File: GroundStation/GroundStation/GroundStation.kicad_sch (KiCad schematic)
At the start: 72 parts, among them J1 SD_Card_Receptacle, J4 Conn_Coaxial, J5 Conn_01x02, P1 USB_C_Plug_USB2.0, Q1 TSM3481CX6 RFG, U1 STM32F103C8Tx, U10 E22-400T30S, U101 LD1117S33TR_SOT223, U11 E80-900M23313S, U4 TPS54538RQFR, U9 NEO-M9N-00B

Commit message: second need freerouting
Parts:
- P1: footprint Connector_USB:USB3_A_Molex_48393-001 -> Connector_USB:USB_C_Receptacle_JAE_DX07S016JA1R1500
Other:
- moved on the sheet: C12, C13, C14, C15, C16, C17, C18, C19, L1, R1, R13, R14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

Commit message: 4/20grounglast
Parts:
- removed C12: 100n, Capacitor_SMD:C_0805_2012Metric_Pad1.18x1.45mm_HandSolder, symbol Device:C
- removed C13, C14, C15: 4.7u, Capacitor_SMD:C_0805_2012Metric_Pad1.18x1.45mm_HandSolder, symbol Device:C
- removed C16: 10p, Capacitor_SMD:C_0805_2012Metric_Pad1.18x1.45mm_HandSolder, symbol Device:C
- removed C17, C18, C19: 47u, Capacitor_SMD:C_0805_2012Metric_Pad1.18x1.45mm_HandSolder, symbol Device:C
- removed C41: NC, Capacitor_SMD:C_0805_2012Metric_Pad1.18x1.45mm_HandSolder, symbol Device:C
- removed C42: 100p, Capacitor_SMD:C_0805_2012Metric_Pad1.18x1.45mm_HandSolder, symbol Device:C
- removed D102, D103: TVS, Diode_SMD:D_SOD-123, symbol Device:D_TVS_Filled
- removed L1: 6.8u, Inductor_SMD:L_0805_2012Metric_Pad1.05x1.20mm_HandSolder, symbol Device:L
- removed L2: short, Inductor_SMD:L_Bourns_SDR0604, symbol Device:L
- removed R1: 390k, Resistor_SMD:R_0805_2012Metric_Pad1.20x1.40mm_HandSolder, symbol Device:R
- removed R13: 18k, Resistor_SMD:R_0805_2012Metric_Pad1.20x1.40mm_HandSolder, symbol Device:R
- removed R14: 220k, Resistor_SMD:R_0805_2012Metric_Pad1.20x1.40mm_HandSolder, symbol Device:R
- removed R15: 30k, Resistor_SMD:R_0805_2012Metric_Pad1.20x1.40mm_HandSolder, symbol Device:R
- removed R16(PG_pull_up)101, R2: 100k, Resistor_SMD:R_0805_2012Metric_Pad1.20x1.40mm_HandSolder, symbol Device:R
- removed R27: NC, Resistor_SMD:R_0805_2012Metric_Pad1.20x1.40mm_HandSolder, symbol Device:R
- removed U4: TPS54538RQFR, RF:TPS54538RQFR, symbol Small_av_tony_lib:TPS54538RQFR
- added BU101: ~, Connector:FanPinHeader_1x03_P2.54mm_Vertical, symbol New_Library_0:BK
- added C101: 330u, Capacitor_SMD:C_0805_2012Metric_Pad1.18x1.45mm_HandSolder, symbol Device:C
- added C102: 22u, Capacitor_SMD:C_0805_2012Metric_Pad1.18x1.45mm_HandSolder, symbol Device:C
- added C103: 2.2u, Capacitor_SMD:C_0805_2012Metric_Pad1.18x1.45mm_HandSolder, symbol Device:C
- added C104: 1u, Capacitor_SMD:C_0805_2012Metric_Pad1.18x1.45mm_HandSolder, symbol Device:C
- added C27, C28: 22pF, Capacitor_SMD:C_0603_1608Metric_Pad1.08x0.95mm_HandSolder, symbol Device:C
- added D102, D104: D_Schottky, Diode_SMD:D_SMA, symbol Device:D_Schottky
- added H101, H102, H103: MountingHole, MountingHole:MountingHole_3.2mm_M3, symbol Mechanical:MountingHole
- added L101, L102: 1mH, Inductor_SMD:L_0805_2012Metric_Pad1.05x1.20mm_HandSolder, symbol Device:L
- added Y1: 8Mhz, Crystal:Crystal_SMD_5032-4Pin_5.0x3.2mm, symbol Device:Crystal_GND24
- J4: footprint Connector_Coaxial:BNC_Amphenol_B6252HB-NPP3G-50_Horizontal -> Connector_Coaxial:U.FL_Hirose_U.FL-R-SMT-1_Vertical
- J5: footprint Connector_PinHeader_2.54mm:PinHeader_1x02_P2.54mm_Horizontal -> Connector_Molex:Molex_Micro-Fit_3.0_43650-0200_1x02_P3.00mm_Horizontal
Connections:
- net +3.3V: now also C10.1, C2.1, C39.1, C40.1, C6.1, C7.1, C8.1, C9.1, J1.4 (VDD), R29.1, R2_up1.1, U1.1 (VBAT), U1.24 (VDD), U1.36 (VDD), U1.48 (VDD), U9.22 (V_BCKP), U9.23 (VCC)
- net BUCK_5V: now also BU101.3 (VOUT), C102.1, D102.2 (A)
- net GND: now also BU101.2 (GND), C102.2, C104.2, C27.2, C28.2, L102.2, Y1.2 (G), Y1.4 (G)
- net USB_5V: now also D104.2 (A)
- net V_BAT+: now also C101.1, C103.1, L101.1
- net HSE_IN: now reaches U1.10 (PA0)
- net HSE_IN: now also C27.1, Y1.1
- net HSE_OUT: now reaches U1.11 (PA1)
- net HSE_OUT: now also C28.1, Y1.3
- net at J4.1 (In): now also U9.11 (RF_IN)
- net at C23.1, U101.3 (VI): now also D102.1 (K), D104.1 (K)
- removed net 3.3V: C10.1, C2.1, C39.1, C40.1, C6.1, C7.1, C8.1, C9.1, FB1.2, J1.4 (VDD), R29.1, R2_up1.1, U1.1 (VBAT), U1.24 (VDD), U1.36 (VDD), U1.48 (VDD), U9.22 (V_BCKP), U9.23 (VCC)
- new net: BU101.1 (VIN), C104.1, L101.2
- new net: C101.2, C103.2, L102.1
- no-connect marks 47 -> 45
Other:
- note added: "HSE crystal"
- moved on the sheet: J4

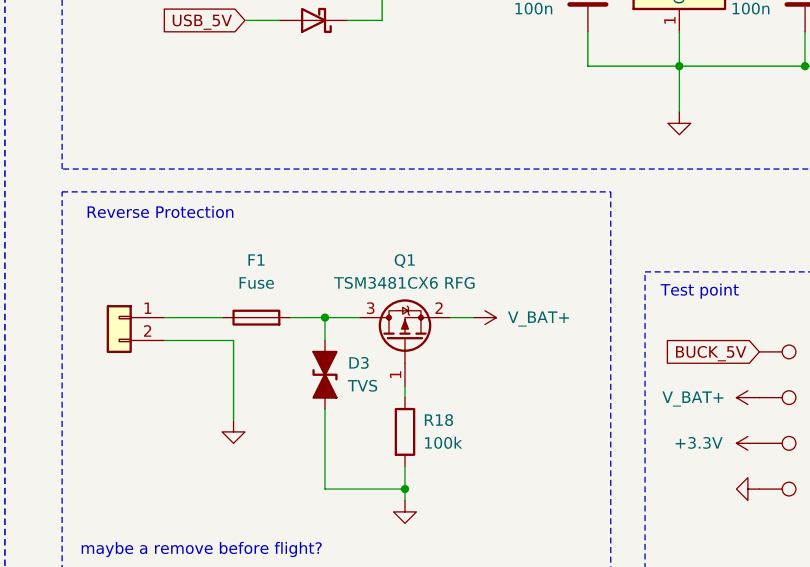
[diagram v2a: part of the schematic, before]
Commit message: change GS MOS
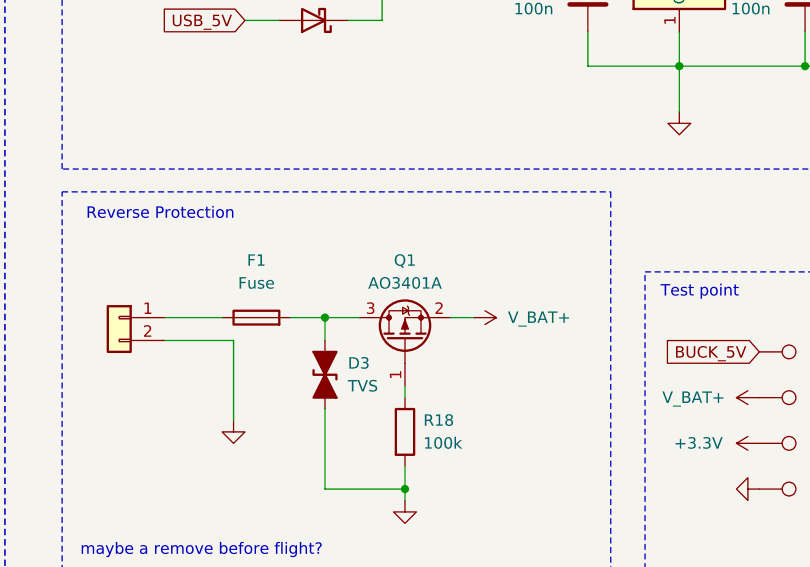
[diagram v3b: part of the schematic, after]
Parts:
- Q1: value TSM3481CX6 RFG -> AO3401A
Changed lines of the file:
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@@
 			)
 		)
-		(property "Value" "TSM3481CX6 RFG"
+		(property "Value" "AO3401A"
 			(at 69.85 328.93 90)
 			(effects

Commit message: 4/25 add some debugger
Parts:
- added C26: 100n, Capacitor_SMD:C_0603_1608Metric_Pad1.08x0.95mm_HandSolder, symbol Device:C
- added J101, J102: Conn_01x02, Connector_PinHeader_2.54mm:PinHeader_1x02_P2.54mm_Vertical, symbol Connector_Generic:Conn_01x02
- added J3: Conn_01x04, Connector_PinHeader_2.54mm:PinHeader_1x04_P2.54mm_Vertical, symbol Connector_Generic:Conn_01x04
- added R3, R4: 10k, Resistor_SMD:R_0805_2012Metric_Pad1.20x1.40mm_HandSolder, symbol Device:R
- added SW1: SW_Push, Button_Switch_THT:SW_PUSH_6mm_H4.3mm, symbol Switch:SW_Push
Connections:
- net +3.3V: now also J101.1 (Pin_1), J3.1 (Pin_1)
- net GND: now also C26.2, J3.4 (Pin_4), R3.2, R4.2, SW1.1
- net USART2_LoRa1_M1: now also U1.39 (PB3); no longer U1.20 (PB2)
- net SWDIO: now reaches U1.34 (PA13)
- net SWDIO: now also J3.2 (Pin_2)
- net SWCLK: now reaches U1.37 (PA14)
- net SWCLK: now also J3.3 (Pin_3)
- net BOOT0: now reaches U1.44 (BOOT0)
- net BOOT0: now also J101.2 (Pin_2), R3.1
- net RESET: now reaches U1.7 (NRST)
- net RESET: now also C26.1, J102.1 (Pin_1), J102.2 (Pin_2), SW1.2
- new net BOOT1: R4.1, U1.20 (PB2)
- no-connect marks 45 -> 40
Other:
- note added: "External reset"
- note added: "Serial Wire Debug"
- note added: "boot mode"
- note added: "go out"

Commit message: Groung garber
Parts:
- removed J102: Conn_01x02, Connector_PinHeader_2.54mm:PinHeader_1x02_P2.54mm_Vertical, symbol Connector_Generic:Conn_01x02
- C101: footprint Capacitor_SMD:C_0805_2012Metric_Pad1.18x1.45mm_HandSolder -> Capacitor_SMD:smd7343
- C22, C24: footprint Capacitor_SMD:C_0805_2012Metric_Pad1.18x1.45mm_HandSolder -> Capacitor_SMD:SMD3528
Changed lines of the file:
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@@
 		)
 	)
-	(global_label "RESET"
-		(shape input)
-		(at 417.83 302.26 180)
-		(fields_autoplaced yes)
-		(effects
-			(font
-				(size 1.27 1.27)
-			)
-			(justify right)
-		)
-		(property "Intersheetrefs" "${INTERSHEET_REFS}"
-			(at 409.0997 302.26 0)
-			(effects
-				(font
-					(size 1.27 1.27)
-				)
-				(justify right)
-				(hide yes)
-			)
-		)
-	)
 	(global_label "USART2_LoRa1_M1"
 		(shape input)
@@
 		)
 	)
-	(global_label "RESET"
-		(shape input)
-		(at 417.83 304.8 180)
-		(fields_autoplaced yes)
-		(effects
-			(font
-				(size 1.27 1.27)
-			)
-			(justify right)
-		)
-		(property "Intersheetrefs" "${INTERSHEET_REFS}"
-			(at 409.0997 304.8 0)
-			(effects
-				(font
-					(size 1.27 1.27)
-				)
-				(justify right)
-				(hide yes)
-			)
-		)
-	)
 	(global_label "USART1_GPS_RX"
 		(shape input)
@@
 	)
 	(symbol
-		(lib_id "Connector_Generic:Conn_01x02")
-		(at 422.91 302.26 0)
-		(unit 1)
-		(exclude_from_sim no)
-		(in_bom yes)
-		(on_board yes)
-		(dnp no)
-		(property "Reference" "J102"
-			(at 417.576 307.848 0)
-			(effects
-				(font
-					(size 1.27 1.27)
-				)
-				(justify left)
-			)
-		)
-		(property "Value" "Conn_01x02"
-			(at 417.576 310.388 0)
-			(effects
-				(font
-					(size 1.27 1.27)
-				)
-				(justify left)
-			)
-		)
-		(property "Footprint" "Connector_PinHeader_2.54mm:PinHeader_1x02_P2.54mm_Vertical"
-			(at 422.91 302.26 0)
-			(effects
-				(font
-					(size 1.27 1.27)
-				)
-				(hide yes)
-			)
-		)
-		(property "Datasheet" "~"
-			(at 422.91 302.26 0)
-			(effects
-				(font
-					(size 1.27 1.27)
-				)
-				(hide yes)
-			)
-		)
-		(property "Description" "Generic connector, single row, 01x02, script generated (kicad-library-utils/schlib/autogen/connector/)"
-			(at 422.91 302.26 0)
-			(effects
-				(font
-					(size 1.27 1.27)
-				)
-				(hide yes)
-			)
-		)
-		(pin "2"
-		)
-		(pin "1"
-		)
-		(instances
-			(project "GroundStation"
-				(path "/5c79a8d7-118d-4f5f-b925-c53bb7ecf529"
-					(reference "J102")
-					(unit 1)
-				)
-			)
-		)
-	)
-	(symbol
 		(lib_id "power:GND")
 		(at 133.35 54.61 0)
@@
 			)
 		)
-		(property "Footprint" "Capacitor_SMD:C_0805_2012Metric_Pad1.18x1.45mm_HandSolder"
+		(property "Footprint" "Capacitor_SMD:SMD3528"
 			(at 124.7648 300.99 0)
 			(effects
@@
 			)
 		)
-		(property "Footprint" "Capacitor_SMD:C_0805_2012Metric_Pad1.18x1.45mm_HandSolder"
+		(property "Footprint" "Capacitor_SMD:smd7343"
 			(at 61.9252 238.76 0)
 			(effects
@@
 			)
 		)
-		(property "Footprint" "Capacitor_SMD:C_0805_2012Metric_Pad1.18x1.45mm_HandSolder"
+		(property "Footprint" "Capacitor_SMD:SMD3528"
 			(at 134.9248 300.99 0)
 			(effects
